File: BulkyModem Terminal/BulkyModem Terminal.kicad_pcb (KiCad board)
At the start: 2 copper layers, 100 x 100 mm, 79 parts, among them J1 DC IN, J2 RS-232, J3 Module_Panel, J4 VGA, J5 TTL, J6 PS/2_Connector, M1 Mounting, M2 Mounting, M3 Mounting, M4 Mounting, Q1 2N3904, Q2 2N7000, Q3 2N7000, SW1 RESET, SW2 DEFAULTS, U1 Pico, U2 74HCT244, U3 MAX232, U5 74HCT04

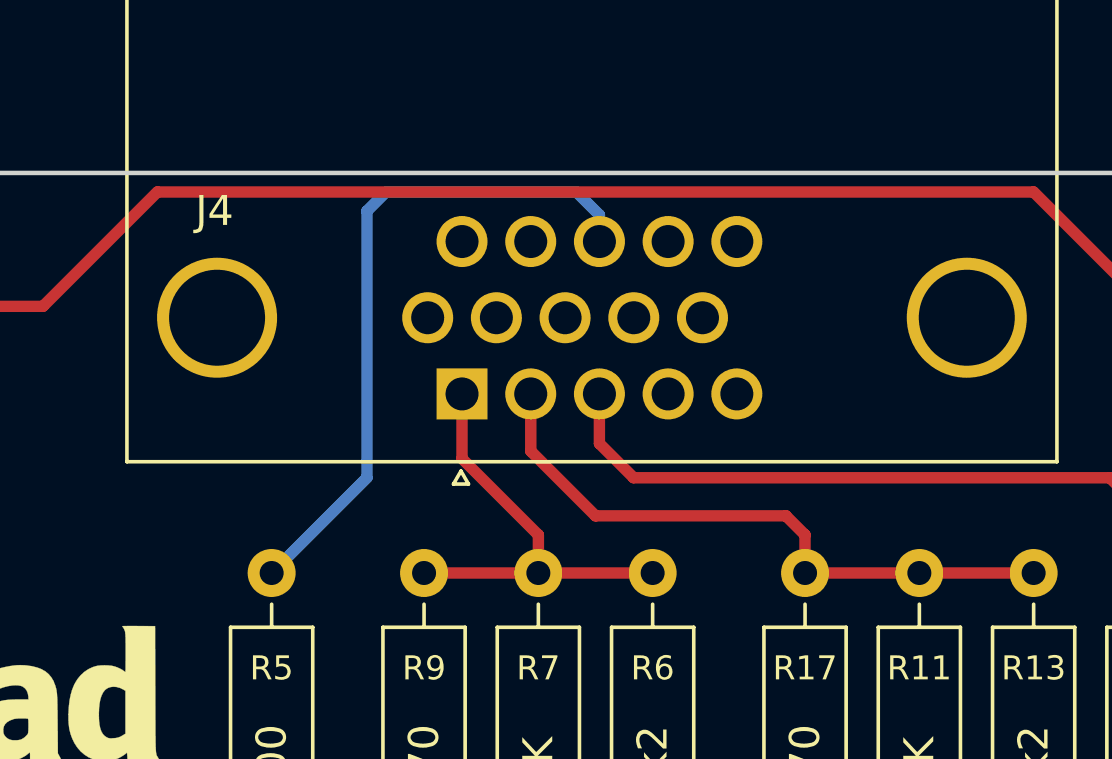
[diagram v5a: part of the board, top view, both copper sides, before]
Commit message: Fixed VGA footprint to match cheap parts
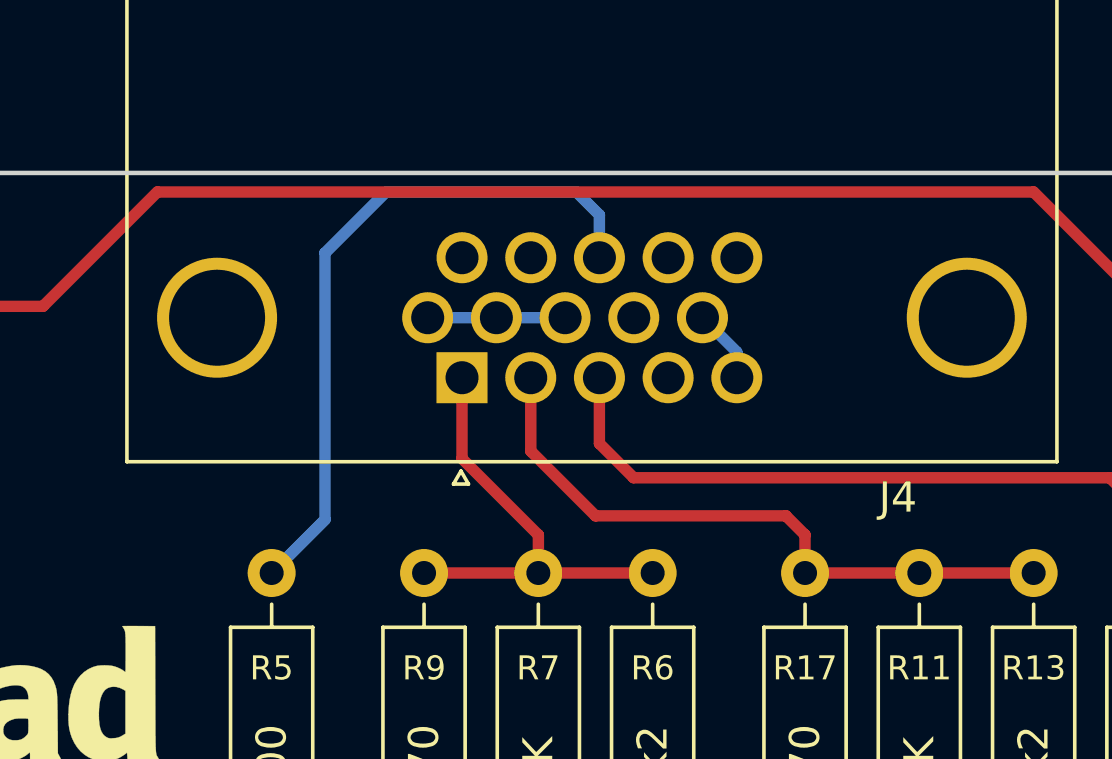
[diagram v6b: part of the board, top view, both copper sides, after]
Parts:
- J4: footprint VGA_DSUB:DSUB-15-L77HDE15SD1CH4F -> VGA_DSUB:DSUB-15
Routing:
- net GND: track 0.00 -> 7.05 mm
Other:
- board text added: "Terminal (rev. C) github.com/tebl"
- board text removed: "Terminal (rev. B) github.com/tebl"
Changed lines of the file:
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@@
 		)
 		(fp_text user "${REFERENCE}"
-			(at 2.54 0 270)
+			(at 2.54 0 -90)
 			(layer "F.Fab")
 			(effects
@@
 		)
 	)
-	(footprint "VGA_DSUB:DSUB-15-L77HDE15SD1CH4F"
+	(footprint "VGA_DSUB:DSUB-15"
 		(layer "F.Cu")
 		(at 145.296 48.006)
-		(descr "15-pin D-Sub connector, horizontal/angled (90 deg), THT-mount, female, pitch 2.29x1.98mm, pin-PCB-offset 3.0300000000000002mm, distance of mounting holes 25mm, distance of mounting holes to PCB edge 4.9399999999999995mm, see https://disti-assets.s3.amazonaws.com/tonar/files/datasheets/16730.pdf")
+		(descr "15-pin D-Sub connector, horizontal/angled (90 deg), THT-mount, female")
 		(tags "15-pin D-Sub connector horizontal angled 90deg THT female pitch 2.29x1.98mm pin-PCB-offset 3.0300000000000002mm mounting-holes-distance 25mm mounting-hole-offset 25mm")
 		(property "Reference" "J4"
-			(at -12.581 7.874 180)
+			(at 10.2 17.43 180)
 			(layer "F.SilkS")
 			(effects
@@
 			)
 		)
-		(property "Footprint" "VGA_DSUB:DSUB-15-L77HDE15SD1CH4F"
-			(at 0 -9.525 0)
+		(property "Footprint" "VGA_DSUB:DSUB-15"
+			(at 0 0 0)
 			(unlocked yes)
 			(layer "F.Fab")
@@
 		)
 		(property "Description" "15-pin female receptacle socket D-SUB connector, High density (3 columns), Triple Row, Generic, VGA-connector, Mounting Hole"
-			(at 0 -11.43 0)
+			(at 0 0 0)
 			(unlocked yes)
 			(layer "F.Fab")
@@
 		)
 		(pad "1" thru_hole rect
-			(at -4.33 13.97 180)
+			(at -4.33 13.43 180)
 			(size 1.7 1.7)
 			(drill 1.1)
@@
 		)
 		(pad "2" thru_hole circle
-			(at -2.04 13.97 180)
+			(at -2.04 13.43 180)
 			(size 1.7 1.7)
 			(drill 1.1)
@@
 		)
 		(pad "3" thru_hole circle
-			(at 0.25 13.97 180)
+			(at 0.25 13.43 180)
 			(size 1.7 1.7)
 			(drill 1.1)
@@
 		)
 		(pad "4" thru_hole circle
-			(at 2.54 13.97 180)
+			(at 2.54 13.43 180)
 			(size 1.7 1.7)
 			(drill 1.1)
@@
 		)
 		(pad "5" thru_hole circle
-			(at 4.83 13.97 180)
+			(at 4.83 13.43 180)
 			(size 1.7 1.7)
 			(drill 1.1)
@@
 		)
 		(pad "11" thru_hole circle
-			(at -4.33 8.89 180)
+			(at -4.33 9.43 180)
 			(size 1.7 1.7)
 			(drill 1.1)
@@
 		)
 		(pad "12" thru_hole circle
-			(at -2.04 8.89 180)
+			(at -2.04 9.43 180)
 			(size 1.7 1.7)
 			(drill 1.1)
@@
 		)
 		(pad "13" thru_hole circle
-			(at 0.25 8.89 180)
+			(at 0.25 9.43 180)
 			(size 1.7 1.7)
 			(drill 1.1)
@@
 		)
 		(pad "14" thru_hole circle
-			(at 2.54 8.89 180)
+			(at 2.54 9.43 180)
 			(size 1.7 1.7)
 			(drill 1.1)
@@
 		)
 		(pad "15" thru_hole circle
-			(at 4.83 8.89 180)
+			(at 4.83 9.43 180)
 			(size 1.7 1.7)
 			(drill 1.1)
@@
 		(model "${KISYS3DMOD}/Connector_Dsub.3dshapes/DSUB-15-HD_Female_Horizontal_P2.29x1.98mm_EdgePinOffset3.03mm_Housed_MountingHolesOffset4.94mm.wrl"
 			(offset
-				(xyz -4.5 -14 0)
+				(xyz 0 0 0)
 			)
 			(scale
@@
 			)
 			(rotate
-				(xyz 0 0 180)
+				(xyz 0 0 0)
 			)
 		)
@@
 		)
 		(fp_text user "${REFERENCE}"
-			(at 2.54 0 270)
+			(at 2.54 0 -90)
 			(layer "F.Fab")
 			(effects
@@
 		)
 	)
-	(gr_text "Terminal (rev. B)\ngithub.com/tebl"
+	(gr_text "Terminal (rev. C)\ngithub.com/tebl"
 		(at 144.145 97.79 0)
 		(layer "B.SilkS")
@@
 	)
 	(segment
+		(start 144.401 59.436)
+		(end 142.111 59.436)
+		(width 0.381)
+		(layer "B.Cu")
+		(net 1)
+	)
+	(segment
+		(start 150.126 61.436)
+		(end 150.126 60.581)
+		(width 0.381)
+		(layer "B.Cu")
+		(net 1)
+	)
+	(segment
+		(start 142.111 59.436)
+		(end 139.821 59.436)
+		(width 0.381)
+		(layer "B.Cu")
+		(net 1)
+	)
+	(segment
+		(start 150.126 60.581)
+		(end 148.981 59.436)
+		(width 0.381)
+		(layer "B.Cu")
+		(net 1)
+	)
+	(segment
 		(start 146.05 129.54)
 		(end 144.78 129.54)
@@
 	)
 	(segment
-		(start 137.795 64.77)
-		(end 137.795 55.88)
+		(start 134.62 67.945)
+		(end 136.398 66.167)
 		(width 0.381)
 		(layer "B.Cu")
@@
 	)
 	(segment
-		(start 145.546 56.011)
-		(end 145.546 56.896)
+		(start 144.78 55.245)
+		(end 145.546 56.011)
 		(width 0.381)
 		(layer "B.Cu")
@@
 	)
 	(segment
-		(start 138.43 55.245)
-		(end 144.78 55.245)
+		(start 136.398 57.277)
+		(end 138.43 55.245)
 		(width 0.381)
 		(layer "B.Cu")
@@
 	)
 	(segment
-		(start 137.795 55.88)
-		(end 138.43 55.245)
+		(start 145.546 56.011)
+		(end 145.546 56.896)
 		(width 0.381)
 		(layer "B.Cu")
@@
 	)
 	(segment
-		(start 134.62 67.945)
-		(end 137.795 64.77)
+		(start 136.398 66.167)
+		(end 136.398 57.277)
 		(width 0.381)
 		(layer "B.Cu")
@@
 	)
 	(segment
-		(start 144.78 55.245)
-		(end 145.546 56.011)
+		(start 138.43 55.245)
+		(end 144.78 55.245)
 		(width 0.381)
 		(layer "B.Cu")

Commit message: Small build tweaks
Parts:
- D1, D3: value 1n4148 -> 1N4148
- R1, R11, R2, R7: value 1K -> 1k
- moved J5 0.10 mm to (87.2, 153.1)
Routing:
- net unconnected-(J6-Pad7)_0: track 0.00 -> 14.2 mm
- net VIN: track 145.2 -> 144.7 mm

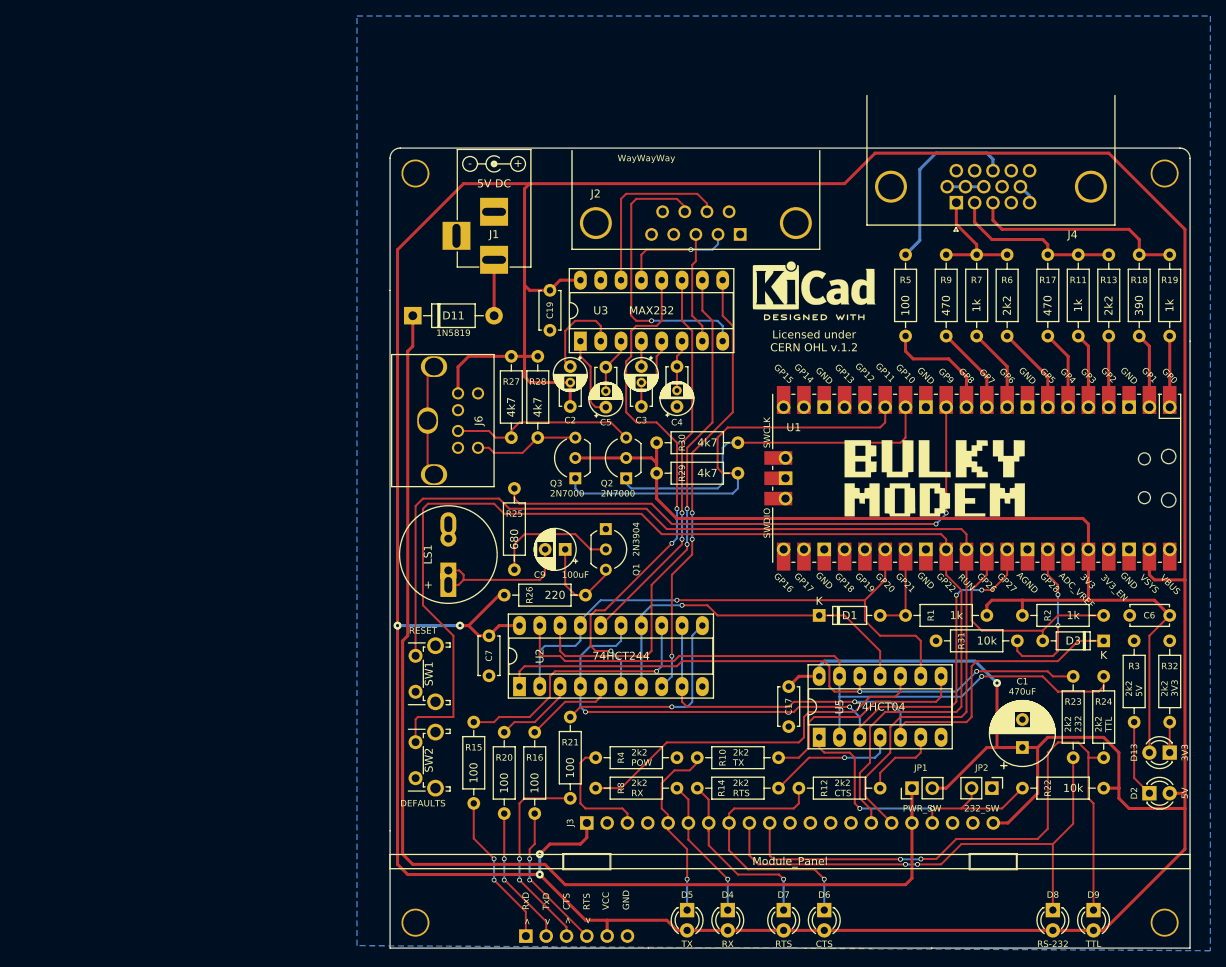
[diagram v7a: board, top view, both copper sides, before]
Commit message: Flipped serial LEDs
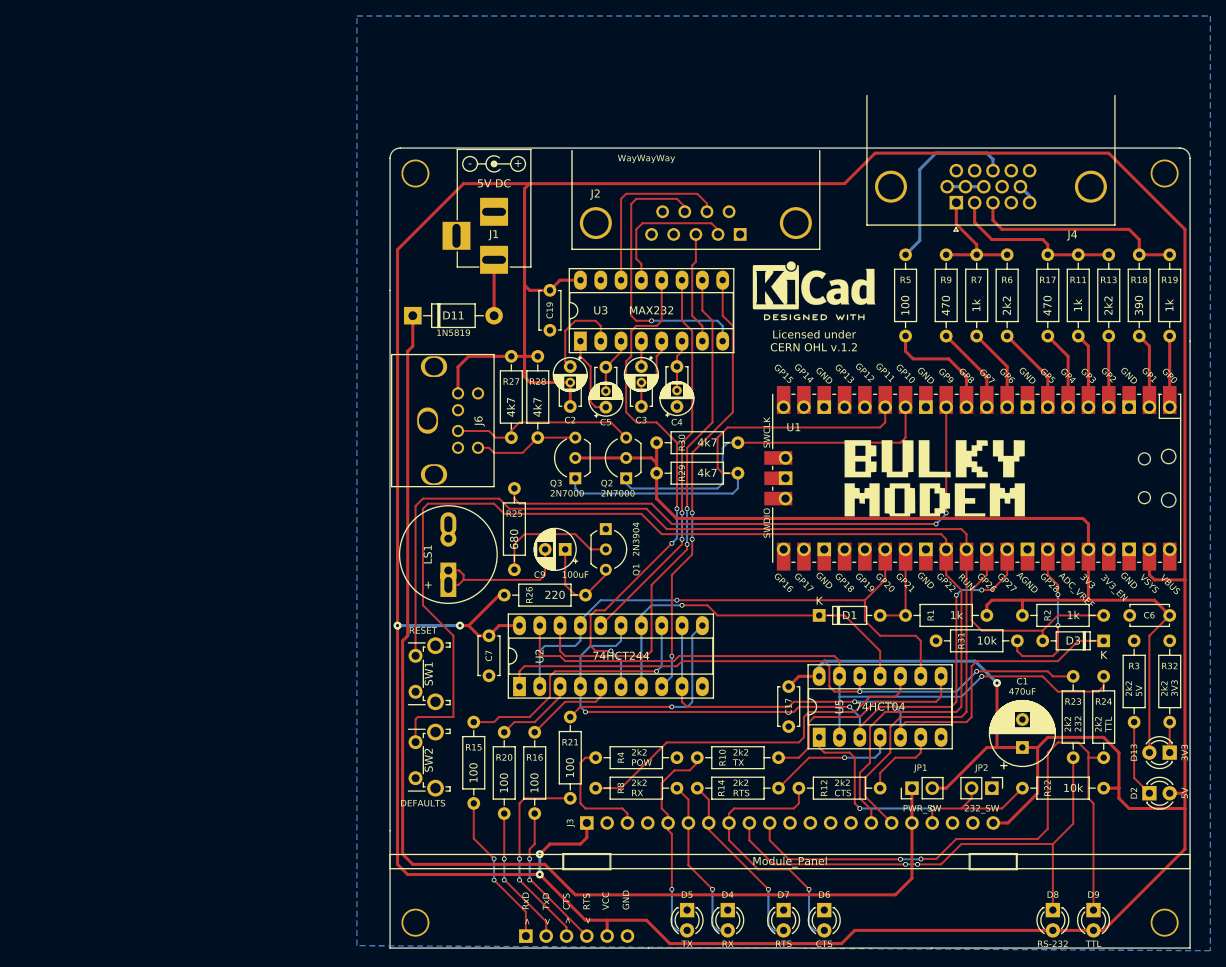
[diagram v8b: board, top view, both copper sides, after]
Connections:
- D4 pad 1: /Front Panel/LED.RX -> GND
- D4 pad 2: +5V -> /Front Panel/LED.RX
- D5 pad 1: /Front Panel/LED.TX -> GND
- D5 pad 2: +5V -> /Front Panel/LED.TX
- D6 pad 1: /Front Panel/LED.CTS -> GND
- D6 pad 2: +5V -> /Front Panel/LED.CTS
- D7 pad 1: /Front Panel/LED.RTS -> GND
- D7 pad 2: +5V -> /Front Panel/LED.RTS
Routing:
- net unconnected-(J6-Pad7)_0: track 14.2 -> 0.00 mm
- net /Serial/DTE.RxD: track 14.5 -> 18.1 mm, vias 1 -> 0
- net /Front Panel/LED.TX: track 22.7 -> 26.0 mm
- net /Front Panel/LED.RX: track 17.9 -> 21.2 mm
- net +5V: track 561.2 -> 562.5 mm
- net /Front Panel/LED.TTL: track 78.1 -> 77.0 mm
- net /Front Panel/LED.232: track 63.6 -> 62.5 mm
- net VIN: track 144.7 -> 145.7 mm
- net /Front Panel/LED.RTS: track 23.7 -> 23.0 mm
- net /Front Panel/LED.CTS: track 33.0 -> 33.7 mm
